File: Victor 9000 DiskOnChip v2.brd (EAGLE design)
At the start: 100 x 80 mm, 9 parts

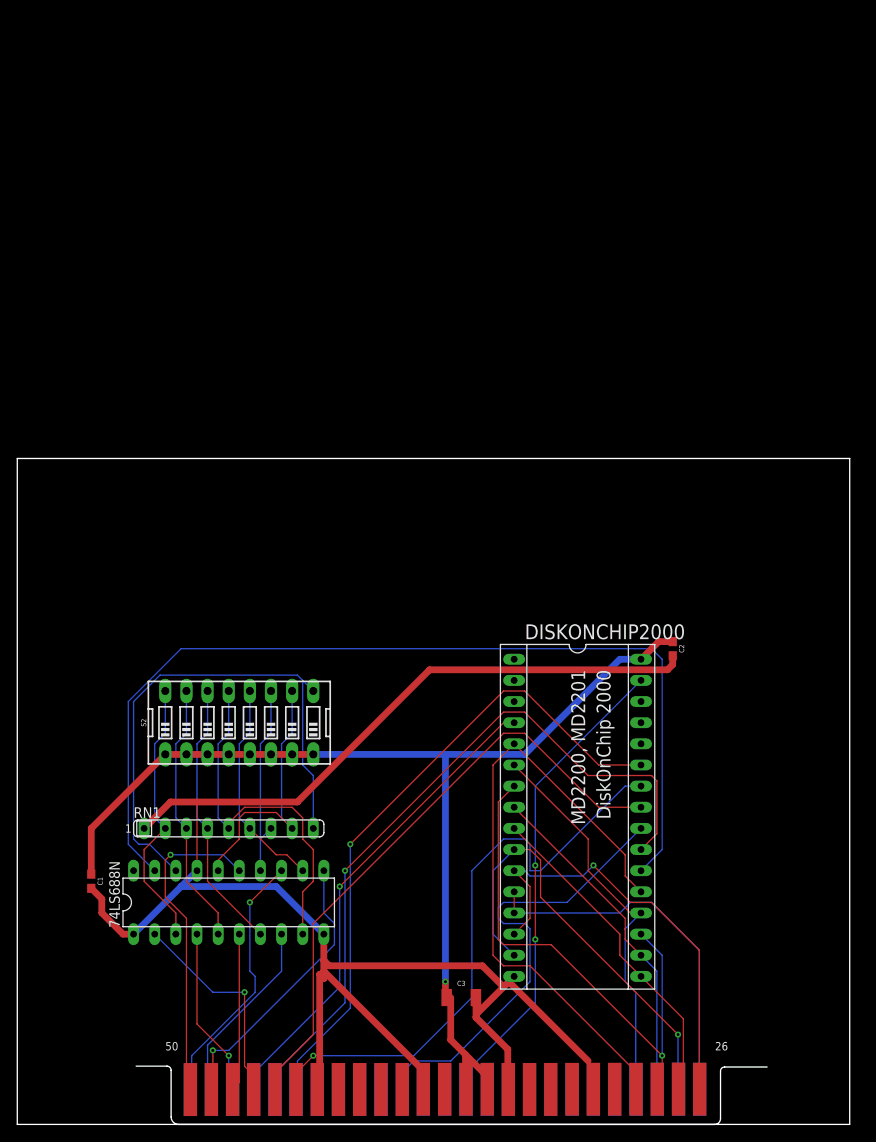
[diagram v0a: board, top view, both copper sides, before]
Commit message: cleaned up schematic
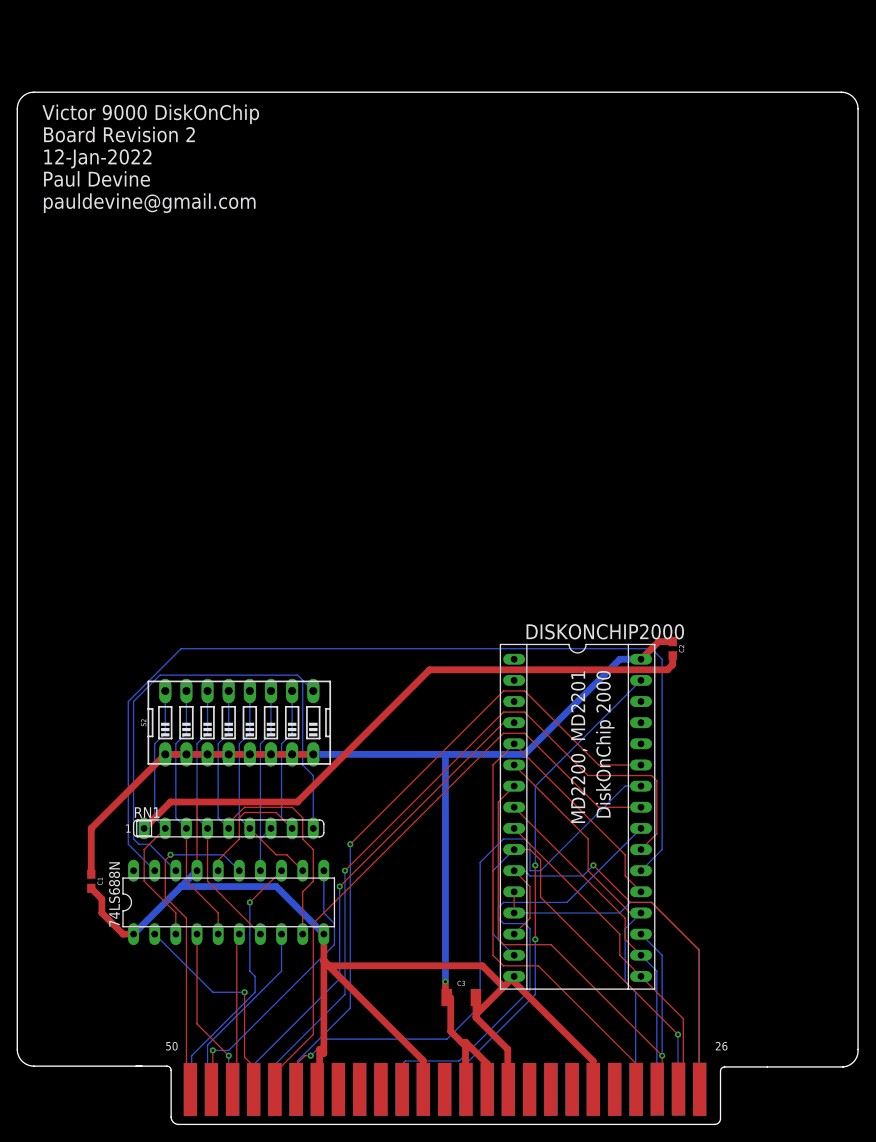
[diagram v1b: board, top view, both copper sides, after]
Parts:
- RN1: value (none) -> Resistor SIP
- S2: value (none) -> DOC Addr Switch
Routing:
- net +5VOLTS: track 132.4 -> 134.3 mm
- net A9: track 71.6 -> 73.4 mm
- net RD: track 54.9 -> 56.1 mm
- net GND: track 218.7 -> 219.8 mm
- net BD7: track 75.6 -> 76.2 mm
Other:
- board size 100 x 80 mm -> 101 x 117.1 mm
- board text added: "TK Add switch to Address values"
- board text added: "Victor 9000 DiskOnChip Board Revision 2 12-Jan-2022 Paul Devine pauldevine@gmail.com"

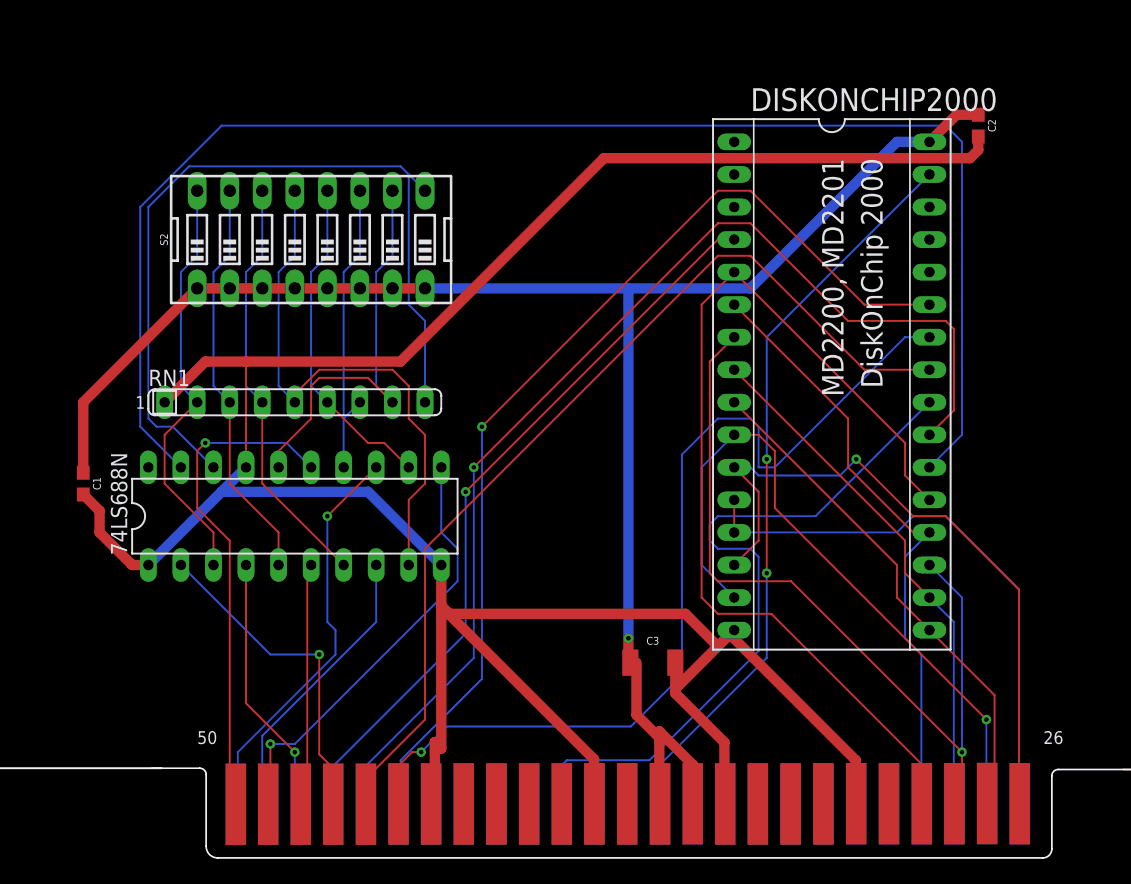
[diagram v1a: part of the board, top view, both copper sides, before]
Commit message: Cleaned up some routing
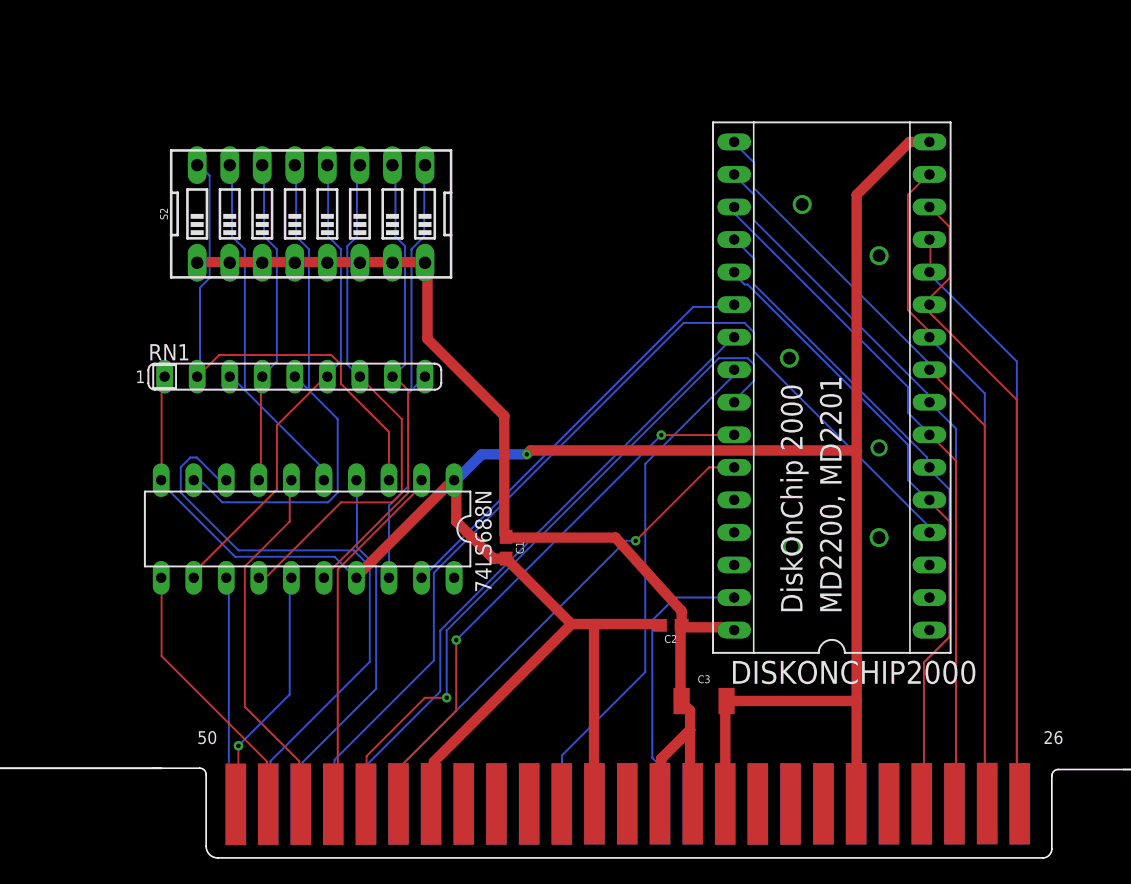
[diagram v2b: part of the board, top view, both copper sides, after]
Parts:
- moved C2 45.8 mm to (54.7, 18.1), turned to 180 degrees
- moved C1 33.4 mm to (41.9, 24.2)
- moved C3 5.00 mm to (57.3, 12.2)
- moved RN1 2.00 mm to (25.4, 37.6)
- moved S2 2.00 mm to (26.7, 50.3)
- moved 74LS688N 1.41 mm to (26.4, 25.7), turned to 180 degrees
- turned DISKONCHIP2000 to 90 degrees
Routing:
- net N$9: track 115.4 -> 33.2 mm
- net +5VOLTS: track 134.3 -> 84.9 mm, vias 1 -> 0
- net A8: track 78.4 -> 38.7 mm
- net A10: track 87.6 -> 48.4 mm, vias 1 -> 0
- net WR: track 57.8 -> 21.7 mm, vias 2 -> 0
- net A9: track 73.4 -> 43.0 mm, vias 1 -> 2
- net N$1: track 65.2 -> 34.9 mm
- net BD7: track 76.2 -> 49.6 mm
- net A16: track 22.6 -> 45.6 mm
- net GND: track 219.8 -> 198.4 mm, vias 0 -> 1
- net A11: track 74.3 -> 53.7 mm, vias 0 -> 1
- net BD3: track 40.1 -> 59.9 mm
- net A19: track 38.8 -> 19.5 mm
- net A12: track 57.8 -> 76.0 mm, vias 1 -> 0
- net N$3: track 23.9 -> 41.7 mm
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
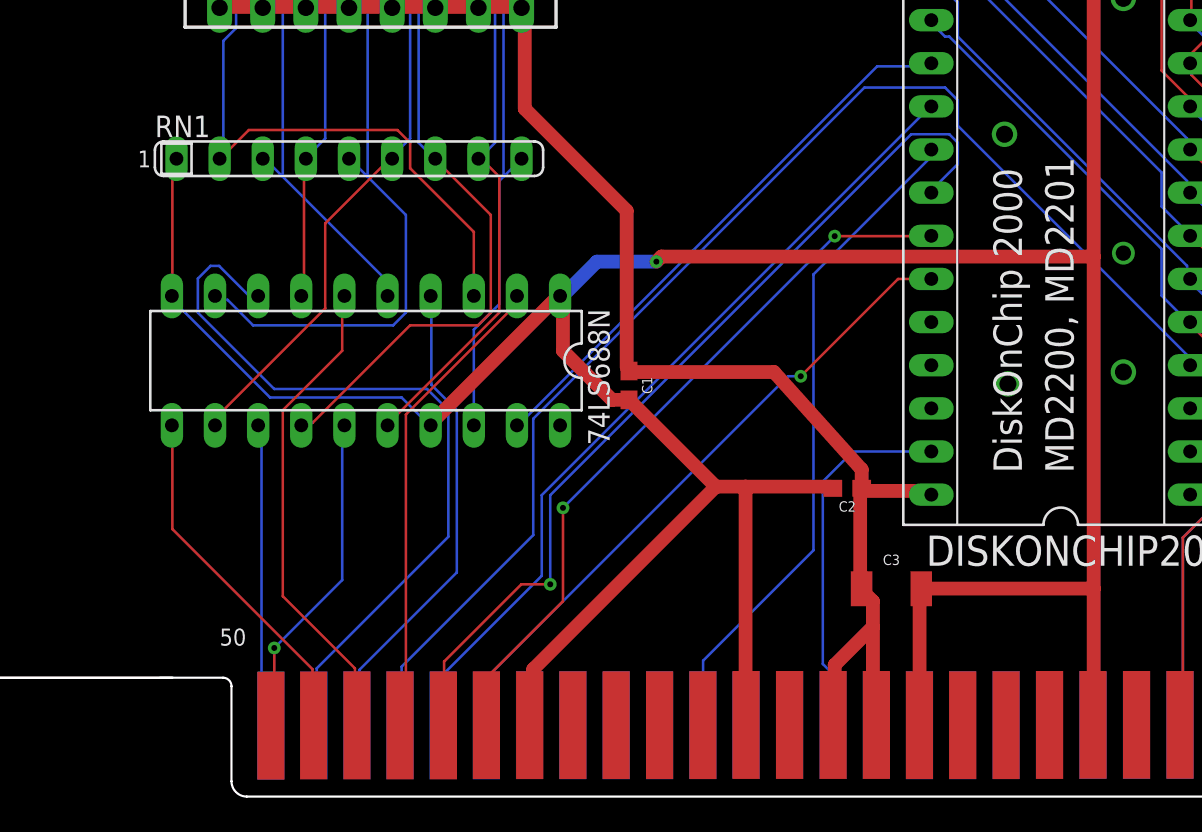
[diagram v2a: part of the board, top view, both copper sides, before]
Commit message: fixed capacitors to be through hole rather than SMD
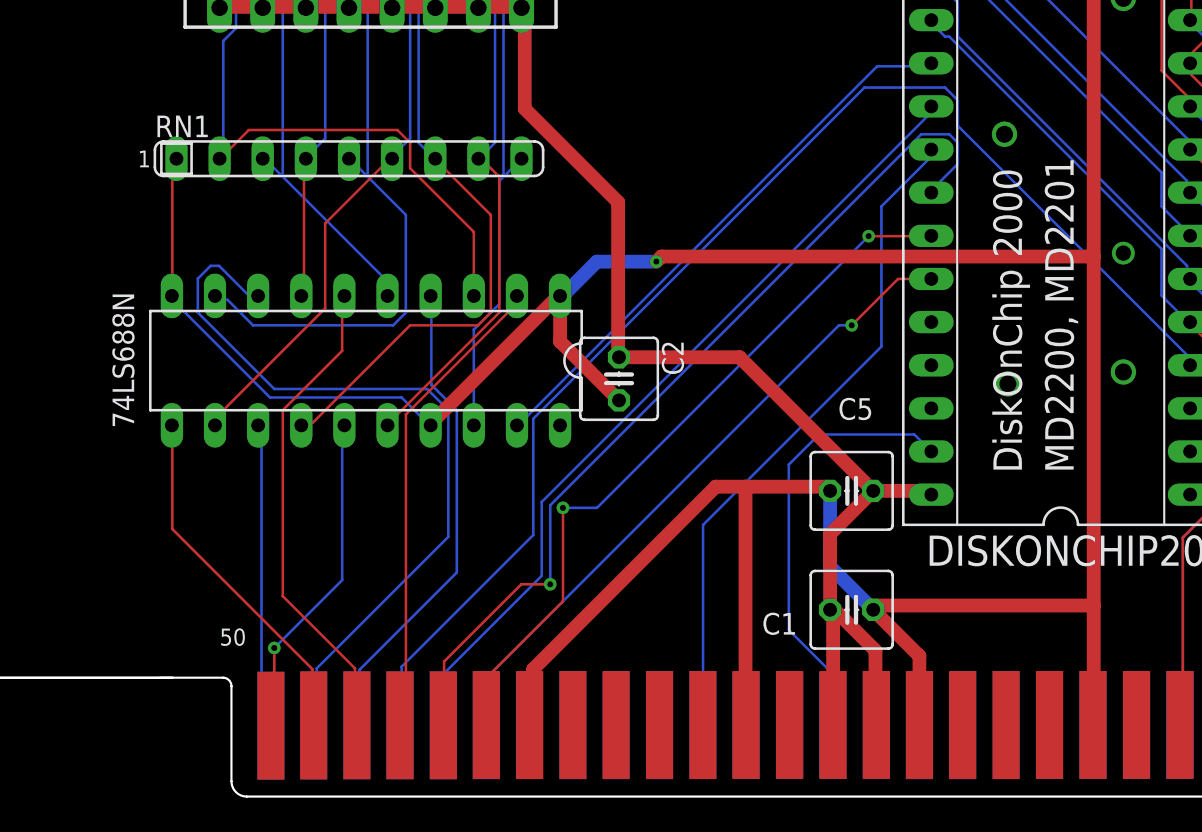
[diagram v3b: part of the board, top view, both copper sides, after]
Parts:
- removed C3: 10uF, SparkFun-Capacitors:1210
- added C5: 0.1uF, rcl:C025-050X050
- C1: value 0.1uF -> 10uf; device SparkFun-Capacitors:0603 -> rcl:C025-050X050
- C2: value 0.1uF -> 0.1uf; device SparkFun-Capacitors:0603 -> rcl:C025-050X050
- moved C1 18.6 mm to (55.0, 11.0), turned to 0 degrees
- moved C2 14.9 mm to (41.3, 24.6), turned to 270 degrees
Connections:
- net +5VOLTS: now also C5.1; no longer C3.1
- net GND: now also C5.2; no longer C3.2
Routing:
- net WR: track 21.7 -> 26.0 mm
- net GND: track 198.4 -> 201.4 mm
- net +5VOLTS: track 84.9 -> 85.9 mm
